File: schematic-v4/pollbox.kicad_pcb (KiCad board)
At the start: 2 copper layers, 50.8 x 74.9 mm, 20 parts, among them P1 CONN_01X15, P10 CONN_01X04, P2 CONN_02X03, P20 CONN_01X04, P3 CONN_01X15, P30 CONN_01X04, P40 CONN_01X04, P50 CONN_01X04, U1 NodeMCU, U2 ULN2803

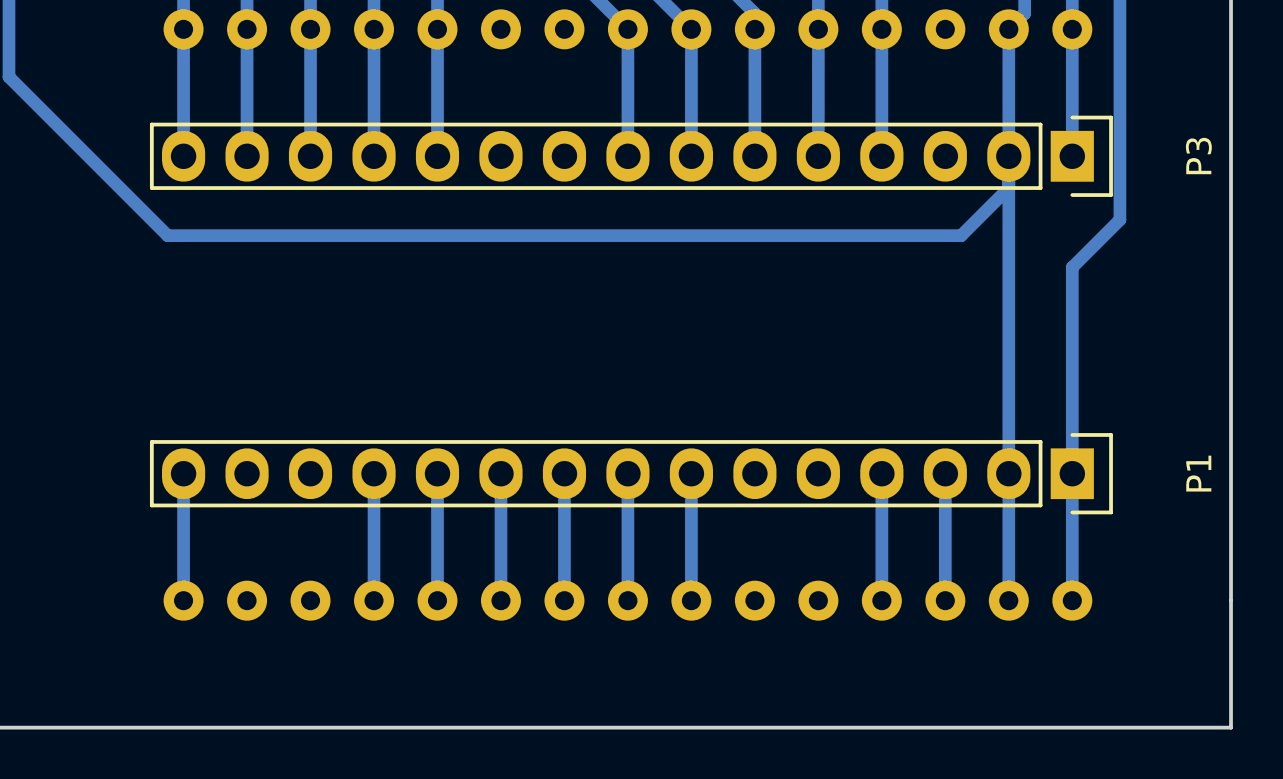
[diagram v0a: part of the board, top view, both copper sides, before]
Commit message: o Support both widths of nodemcu boards. o Adding USB label for correct placement.
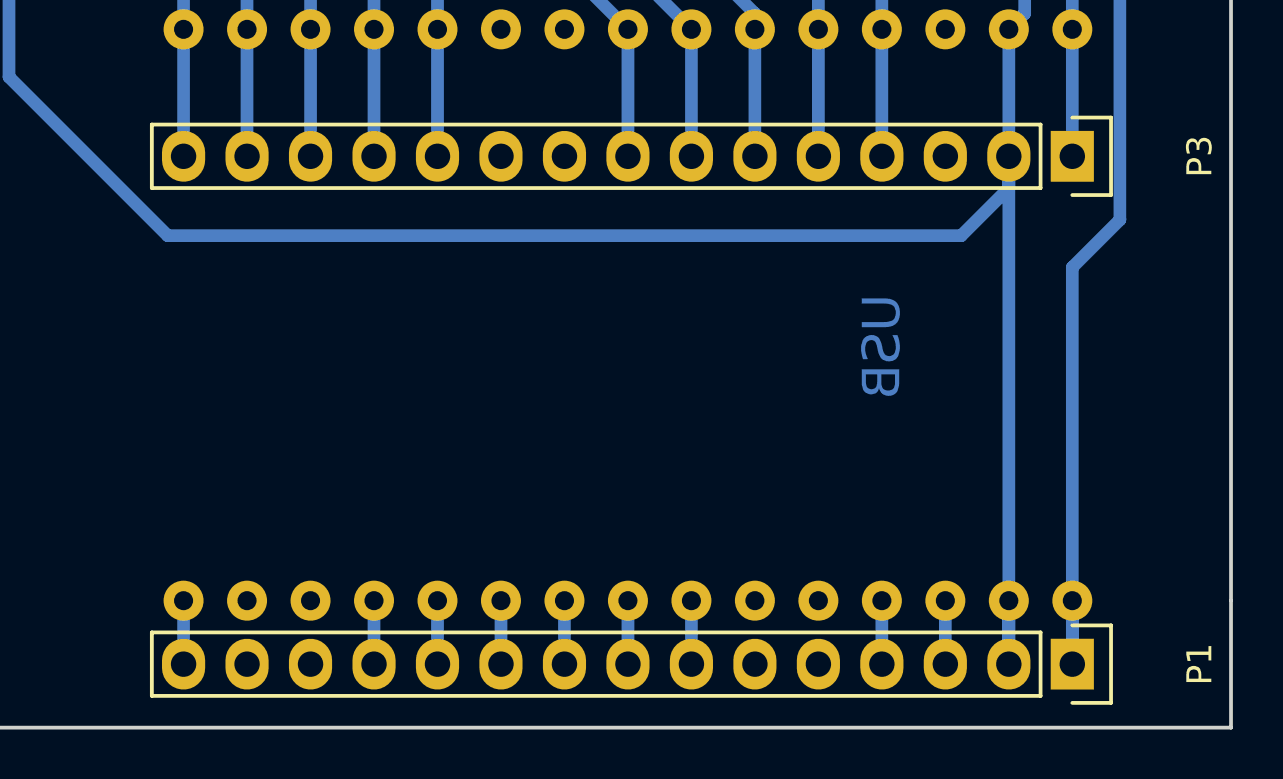
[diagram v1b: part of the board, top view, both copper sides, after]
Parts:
- moved P1 7.62 mm to (121.9, 116.8)
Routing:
- net GND: track 161.6 -> 166.7 mm
- net +5V: track 100.4 -> 105.5 mm
- net /~RST: track 5.08 -> 2.54 mm
- net /SD3: track 5.08 -> 2.54 mm
- net /SD2: track 5.08 -> 2.54 mm
- net /SD1: track 5.08 -> 2.54 mm
- net /SD0: track 5.08 -> 2.54 mm
- net /EN: track 5.08 -> 2.54 mm
- net /CMD: track 5.08 -> 2.54 mm
- net /CLK: track 5.08 -> 2.54 mm
- net /AD0: track 5.08 -> 2.54 mm
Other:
- board text added: "USB"

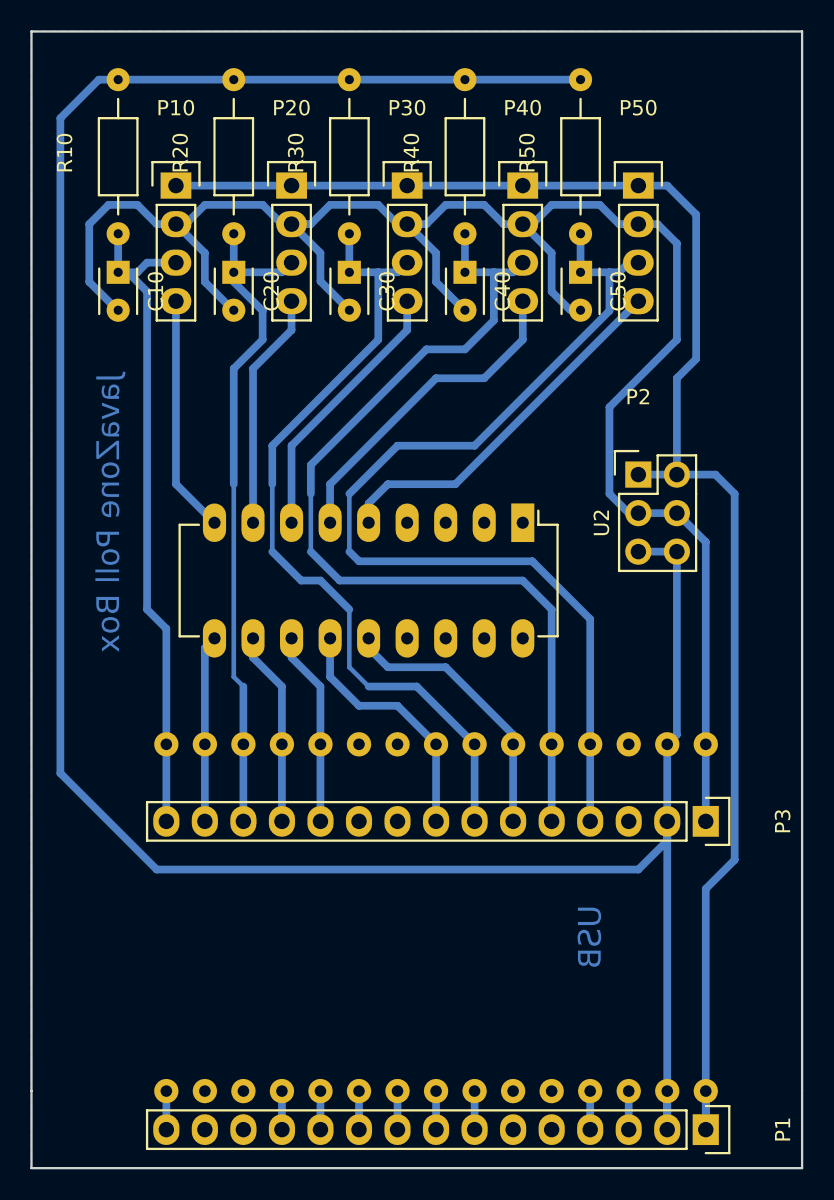
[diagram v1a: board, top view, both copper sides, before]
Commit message: o Filling zones. o Adding drill holes.
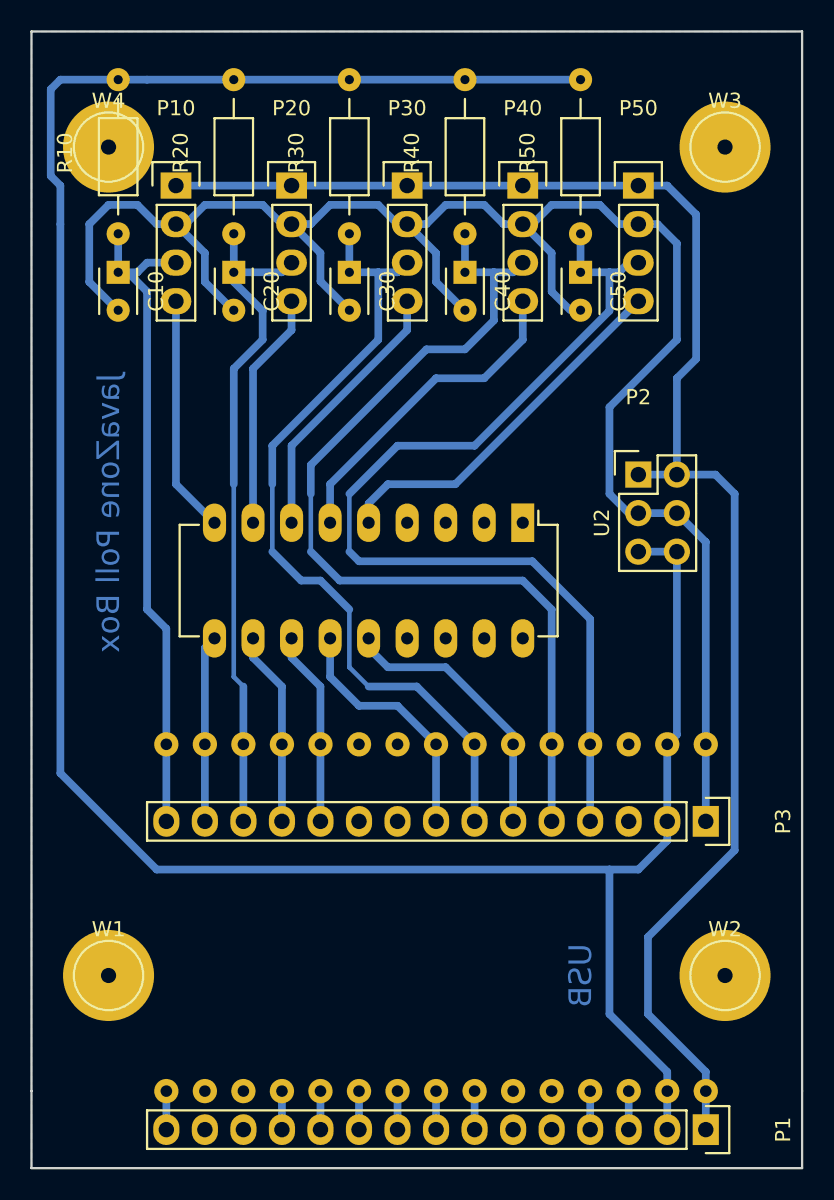
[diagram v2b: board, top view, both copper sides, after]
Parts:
- added W1: TEST_1P, Connect:1pin, F.Cu at (82.5, 106.7)
- added W2: TEST_1P, Connect:1pin, F.Cu at (123.2, 106.7)
- added W3: TEST_1P, Connect:1pin, F.Cu at (123.2, 52.1)
- added W4: TEST_1P, Connect:1pin, F.Cu at (82.5, 52.1)
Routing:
- net GND: track 166.7 -> 164.5 mm
- net +5V: track 105.5 -> 106.1 mm
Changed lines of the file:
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@@
     (links 75)
     (no_connects 0)
-    (area 77.394999 44.374999 128.345001 119.455001)
+    (area 62.814287 35.885 128.345001 122.002333)
     (thickness 1.6)
     (drawings 10)
-    (tracks 208)
+    (tracks 217)
     (zones 0)
-    (modules 20)
+    (modules 24)
     (nets 28)
   )
@@
     (mod_text_size 1 1)
     (mod_text_width 0.15)
-    (pad_size 1.524 1.524)
-    (pad_drill 0.6)
+    (pad_size 6 6)
+    (pad_drill 1)
     (pad_to_mask_clearance 0.2)
     (aux_axis_origin 0 0)
-    (grid_origin 118.11 74.93)
-    (visible_elements FFFCBF7F)
+    (grid_origin 77.47 119.38)
+    (visible_elements FFFCFF7F)
     (pcbplotparams
       (layerselection 0x01000_80000000)
@@
       (outputformat 2)
       (mirror false)
-      (drillshape 1)
+      (drillshape 0)
       (scaleselection 1)
       (outputdirectory ps))
@@
     )
   )
-  (gr_text USB (at 114.3 104.14 90) (layer B.Cu)
+  (module Connect:1pin (layer F.Cu)
+    (at 82.55 106.68)
+    (descr "module 1 pin (ou trou mecanique de percage)")
+    (tags DEV)
+    (fp_text reference W1 (at 0 -3.048) (layer F.SilkS)
+      (effects (font (size 1 1) (thickness 0.15)))
+    )
+    (fp_text value TEST_1P (at 0 2.794) (layer F.Fab)
+      (effects (font (size 1 1) (thickness 0.15)))
+    )
+    (fp_circle (center 0 0) (end 0 -2.286) (layer F.SilkS) (width 0.15))
+    (pad 1 thru_hole circle (at 0 0) (size 6 6) (drill 1) (layers *.Cu *.Mask F.SilkS))
+  )
+  (module Connect:1pin (layer F.Cu)
+    (at 123.19 106.68)
+    (descr "module 1 pin (ou trou mecanique de percage)")
+    (tags DEV)
+    (fp_text reference W2 (at 0 -3.048) (layer F.SilkS)
+      (effects (font (size 1 1) (thickness 0.15)))
+    )
+    (fp_text value TEST_1P (at 0 2.794) (layer F.Fab)
+      (effects (font (size 1 1) (thickness 0.15)))
+    )
+    (fp_circle (center 0 0) (end 0 -2.286) (layer F.SilkS) (width 0.15))
+    (pad 1 thru_hole circle (at 0 0) (size 6 6) (drill 1) (layers *.Cu *.Mask F.SilkS))
+  )
+  (module Connect:1pin (layer F.Cu)
+    (at 123.19 52.07)
+    (descr "module 1 pin (ou trou mecanique de percage)")
+    (tags DEV)
+    (fp_text reference W3 (at 0 -3.048) (layer F.SilkS)
+      (effects (font (size 1 1) (thickness 0.15)))
+    )
+    (fp_text value TEST_1P (at 0 2.794) (layer F.Fab)
+      (effects (font (size 1 1) (thickness 0.15)))
+    )
+    (fp_circle (center 0 0) (end 0 -2.286) (layer F.SilkS) (width 0.15))
+    (pad 1 thru_hole circle (at 0 0) (size 6 6) (drill 1) (layers *.Cu *.Mask F.SilkS))
+  )
+  (module Connect:1pin (layer F.Cu)
+    (at 82.55 52.07)
+    (descr "module 1 pin (ou trou mecanique de percage)")
+    (tags DEV)
+    (fp_text reference W4 (at 0 -3.048) (layer F.SilkS)
+      (effects (font (size 1 1) (thickness 0.15)))
+    )
+    (fp_text value TEST_1P (at 0 2.794) (layer F.Fab)
+      (effects (font (size 1 1) (thickness 0.15)))
+    )
+    (fp_circle (center 0 0) (end 0 -2.286) (layer F.SilkS) (width 0.15))
+    (pad 1 thru_hole circle (at 0 0) (size 6 6) (drill 1) (layers *.Cu *.Mask F.SilkS))
+  )
+  (gr_text USB (at 113.665 106.68 90) (layer B.Cu)
     (effects (font (size 1.5 1.5) (thickness 0.3)) (justify mirror))
   )
@@
   (segment (start 92.71 55.88) (end 93.98 57.15) (width 0.508) (layer B.Cu) (net 1) (status 20))
   (segment (start 93.98 57.15) (end 94.615 57.15) (width 0.508) (layer B.Cu) (net 1) (status 30))
-  (segment (start 120.015 73.66) (end 120.015 67.31) (width 0.508) (layer B.Cu) (net 2))
-  (segment (start 119.38 54.61) (end 117.475 54.61) (width 0.508) (layer B.Cu) (net 2))
-  (segment (start 121.285 56.515) (end 119.38 54.61) (width 0.508) (layer B.Cu) (net 2))
-  (segment (start 121.285 66.04) (end 121.285 56.515) (width 0.508) (layer B.Cu) (net 2))
-  (segment (start 120.015 67.31) (end 121.285 66.04) (width 0.508) (layer B.Cu) (net 2))
-  (segment (start 121.92 116.84) (end 121.92 100.965) (width 0.508) (layer B.Cu) (net 2) (status 10))
+  (segment (start 121.92 114.3) (end 121.92 113.03) (width 0.508) (layer B.Cu) (net 2))
+  (segment (start 118.11 104.14) (end 123.825 98.425) (width 0.508) (layer B.Cu) (net 2))
+  (segment (start 118.11 109.22) (end 118.11 104.14) (width 0.508) (layer B.Cu) (net 2))
+  (segment (start 121.92 113.03) (end 118.11 109.22) (width 0.508) (layer B.Cu) (net 2))
+  (segment (start 123.825 98.425) (end 123.825 74.93) (width 0.508) (layer B.Cu) (net 2))
   (segment (start 122.555 73.66) (end 120.015 73.66) (width 0.508) (layer B.Cu) (net 2))
   (segment (start 123.825 74.93) (end 122.555 73.66) (width 0.508) (layer B.Cu) (net 2))
-  (segment (start 123.825 99.06) (end 123.825 74.93) (width 0.508) (layer B.Cu) (net 2))
-  (segment (start 121.92 100.965) (end 123.825 99.06) (width 0.508) (layer B.Cu) (net 2))
+  (segment (start 120.015 73.66) (end 120.015 67.31) (width 0.508) (layer B.Cu) (net 2))
+  (segment (start 120.015 67.31) (end 121.285 66.04) (width 0.508) (layer B.Cu) (net 2))
+  (segment (start 121.285 66.04) (end 121.285 56.515) (width 0.508) (layer B.Cu) (net 2))
+  (segment (start 121.285 56.515) (end 119.38 54.61) (width 0.508) (layer B.Cu) (net 2))
+  (segment (start 119.38 54.61) (end 117.475 54.61) (width 0.508) (layer B.Cu) (net 2))
   (segment (start 117.475 73.66) (end 120.015 73.66) (width 0.508) (layer B.Cu) (net 2))
   (segment (start 121.92 116.84) (end 121.92 114.3) (width 0.508) (layer B.Cu) (net 2) (status 10))
@@
   (segment (start 102.235 54.61) (end 109.855 54.61) (width 0.508) (layer B.Cu) (net 2) (status 30))
   (segment (start 94.615 54.61) (end 102.235 54.61) (width 0.508) (layer B.Cu) (net 2) (status 30))
-  (segment (start 119.38 116.84) (end 119.38 96.52) (width 0.508) (layer B.Cu) (net 3) (status 10))
+  (segment (start 119.38 114.3) (end 119.38 113.03) (width 0.508) (layer B.Cu) (net 3))
+  (segment (start 115.57 109.22) (end 115.57 99.695) (width 0.508) (layer B.Cu) (net 3))
+  (segment (start 119.38 113.03) (end 115.57 109.22) (width 0.508) (layer B.Cu) (net 3))
+  (segment (start 79.375 57.15) (end 79.375 54.61) (width 0.508) (layer B.Cu) (net 3))
+  (segment (start 79.375 54.61) (end 78.74 53.975) (width 0.508) (layer B.Cu) (net 3))
+  (segment (start 78.74 53.975) (end 78.74 48.26) (width 0.508) (layer B.Cu) (net 3))
+  (segment (start 78.74 48.26) (end 79.375 47.625) (width 0.508) (layer B.Cu) (net 3))
+  (segment (start 79.375 47.625) (end 83.185 47.625) (width 0.508) (layer B.Cu) (net 3))
+  (segment (start 115.57 99.695) (end 85.725 99.695) (width 0.508) (layer B.Cu) (net 3))
+  (segment (start 79.375 93.345) (end 79.375 57.15) (width 0.508) (layer B.Cu) (net 3))
+  (segment (start 85.725 99.695) (end 79.375 93.345) (width 0.508) (layer B.Cu) (net 3))
+  (segment (start 117.475 99.695) (end 115.57 99.695) (width 0.508) (layer B.Cu) (net 3))
+  (segment (start 119.38 97.79) (end 117.475 99.695) (width 0.508) (layer B.Cu) (net 3))
   (segment (start 119.38 96.52) (end 119.38 97.79) (width 0.508) (layer B.Cu) (net 3))
-  (segment (start 119.38 97.79) (end 117.475 99.695) (width 0.508) (layer B.Cu) (net 3))
-  (segment (start 117.475 99.695) (end 85.725 99.695) (width 0.508) (layer B.Cu) (net 3))
-  (segment (start 85.725 99.695) (end 79.375 93.345) (width 0.508) (layer B.Cu) (net 3))
-  (segment (start 79.375 93.345) (end 79.375 50.165) (width 0.508) (layer B.Cu) (net 3))
-  (segment (start 79.375 50.165) (end 81.915 47.625) (width 0.508) (layer B.Cu) (net 3))
-  (segment (start 81.915 47.625) (end 83.185 47.625) (width 0.508) (layer B.Cu) (net 3))
   (segment (start 120.015 78.74) (end 120.015 90.805) (width 0.508) (layer B.Cu) (net 3))
   (segment (start 120.015 90.805) (end 119.38 91.44) (width 0.508) (layer B.Cu) (net 3) (status 20))
@@
   (segment (start 106.045 47.625) (end 113.665 47.625) (width 0.508) (layer B.Cu) (net 3) (status 30))
   (segment (start 98.425 47.625) (end 106.045 47.625) (width 0.508) (layer B.Cu) (net 3) (status 30))
-  (segment (start 83.185 47.625) (end 90.805 47.625) (width 0.508) (layer B.Cu) (net 3) (status 30))
+  (segment (start 83.185 47.625) (end 85.09 47.625) (width 0.508) (layer B.Cu) (net 3) (status 30))
+  (segment (start 85.09 47.625) (end 90.805 47.625) (width 0.508) (layer B.Cu) (net 3) (status 30))
   (segment (start 86.995 62.23) (end 86.995 74.295) (width 0.508) (layer B.Cu) (net 4) (status 10))
   (segment (start 86.995 74.295) (end 89.535 76.835) (width 0.508) (layer B.Cu) (net 4) (status 20))
@@
     (connect_pads (clearance 0.508))
     (min_thickness 0.254)
-    (fill (arc_segments 16) (thermal_gap 0.508) (thermal_bridge_width 0.508))
+    (fill yes (arc_segments 16) (thermal_gap 0.508) (thermal_bridge_width 0.508))
     (polygon
       (pts
